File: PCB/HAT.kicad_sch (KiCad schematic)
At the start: 0 parts

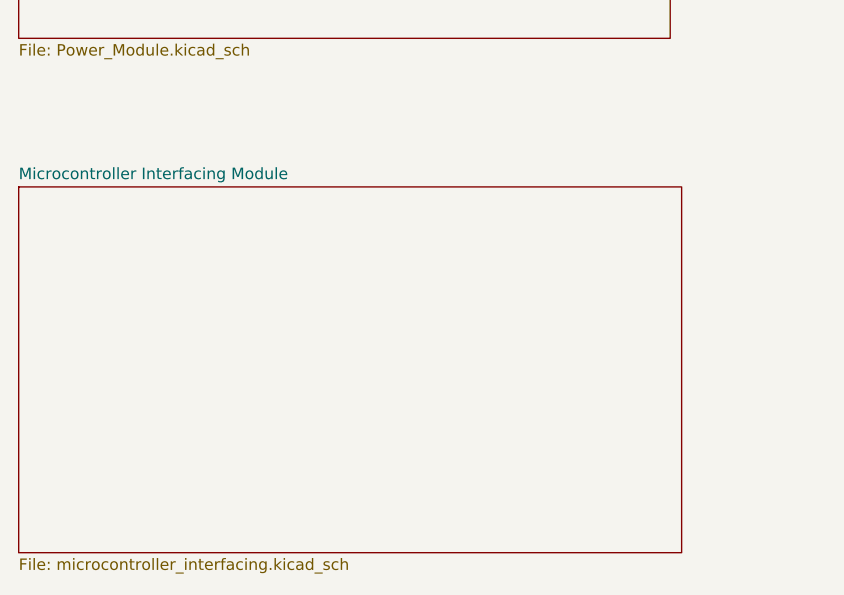
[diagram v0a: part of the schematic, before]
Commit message: Revert "Add microcontroller interfacing schematic"
This reverts commit cb65be9f095c25773123ea45fc6a49ffd102fb8b.
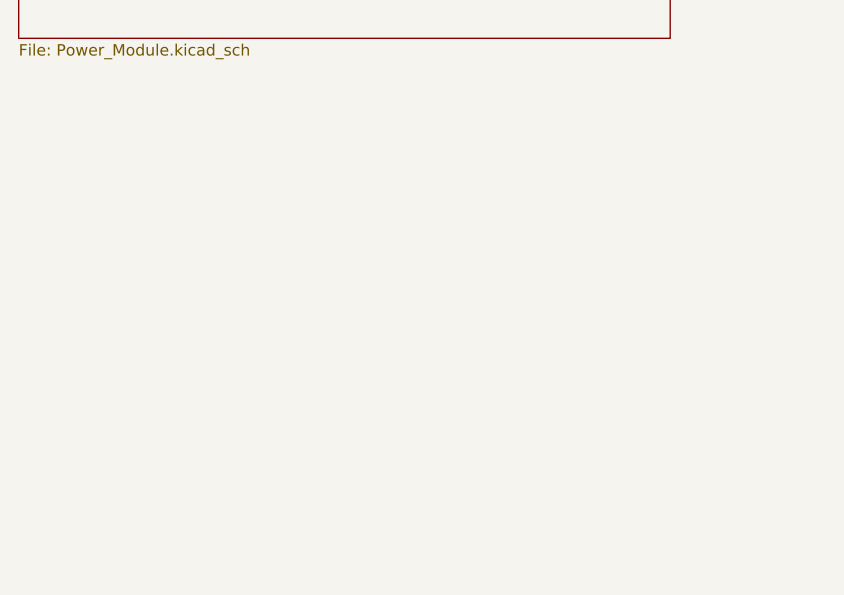
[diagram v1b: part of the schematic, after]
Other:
- removed sheet Microcontroller Interfacing Module
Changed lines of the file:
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@@
-    )
-  )
-  (sheet (at 40.64 83.82) (size 73.66 40.64) (fields_autoplaced)
-    (stroke (width 0.1524) (type solid))
-    (fill (color 0 0 0 0.0000))
-    (property "Sheetname" "Microcontroller Interfacing Module" (at 40.64 83.1084 0)
-      (effects (font (size 1.27 1.27)) (justify left bottom))
-    )
-    (property "Sheetfile" "microcontroller_interfacing.kicad_sch" (at 40.64 125.0446 0)
-      (effects (font (size 1.27 1.27)) (justify left top))
-    )
-    (instances
-      (project "HAT"
-        (path "/40f36b19-a08c-43e7-88a6-ec8387939712" (page "4"))
-      )
     )
   )

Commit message: Add microcontroller interfacing schematic
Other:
- added sheet Microcontroller Interfacing Module (microcontroller_interfacing.kicad_sch)
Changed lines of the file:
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@@
+    )
+  )
+  (sheet (at 40.64 83.82) (size 73.66 40.64) (fields_autoplaced)
+    (stroke (width 0.1524) (type solid))
+    (fill (color 0 0 0 0.0000))
+    (property "Sheetname" "Microcontroller Interfacing Module" (at 40.64 83.1084 0)
+      (effects (font (size 1.27 1.27)) (justify left bottom))
+    )
+    (property "Sheetfile" "microcontroller_interfacing.kicad_sch" (at 40.64 125.0446 0)
+      (effects (font (size 1.27 1.27)) (justify left top))
+    )
+    (instances
+      (project "HAT"
+        (path "/40f36b19-a08c-43e7-88a6-ec8387939712" (page "4"))
+      )
     )
   )
